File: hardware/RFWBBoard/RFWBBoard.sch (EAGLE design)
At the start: 123 parts, among them IC1 24LC025ST, J1 CON-71742-3003-BOT, M1 MOUNT-HOLE3.3, M2 MOUNT-HOLE3.3, M3 MOUNT-HOLE3.3, M4 MOUNT-HOLE3.3, M5 FIDUCIAL1X2, M6 FIDUCIAL1X2, M7 FIDUCIAL1X2, M8 FIDUCIAL1X2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

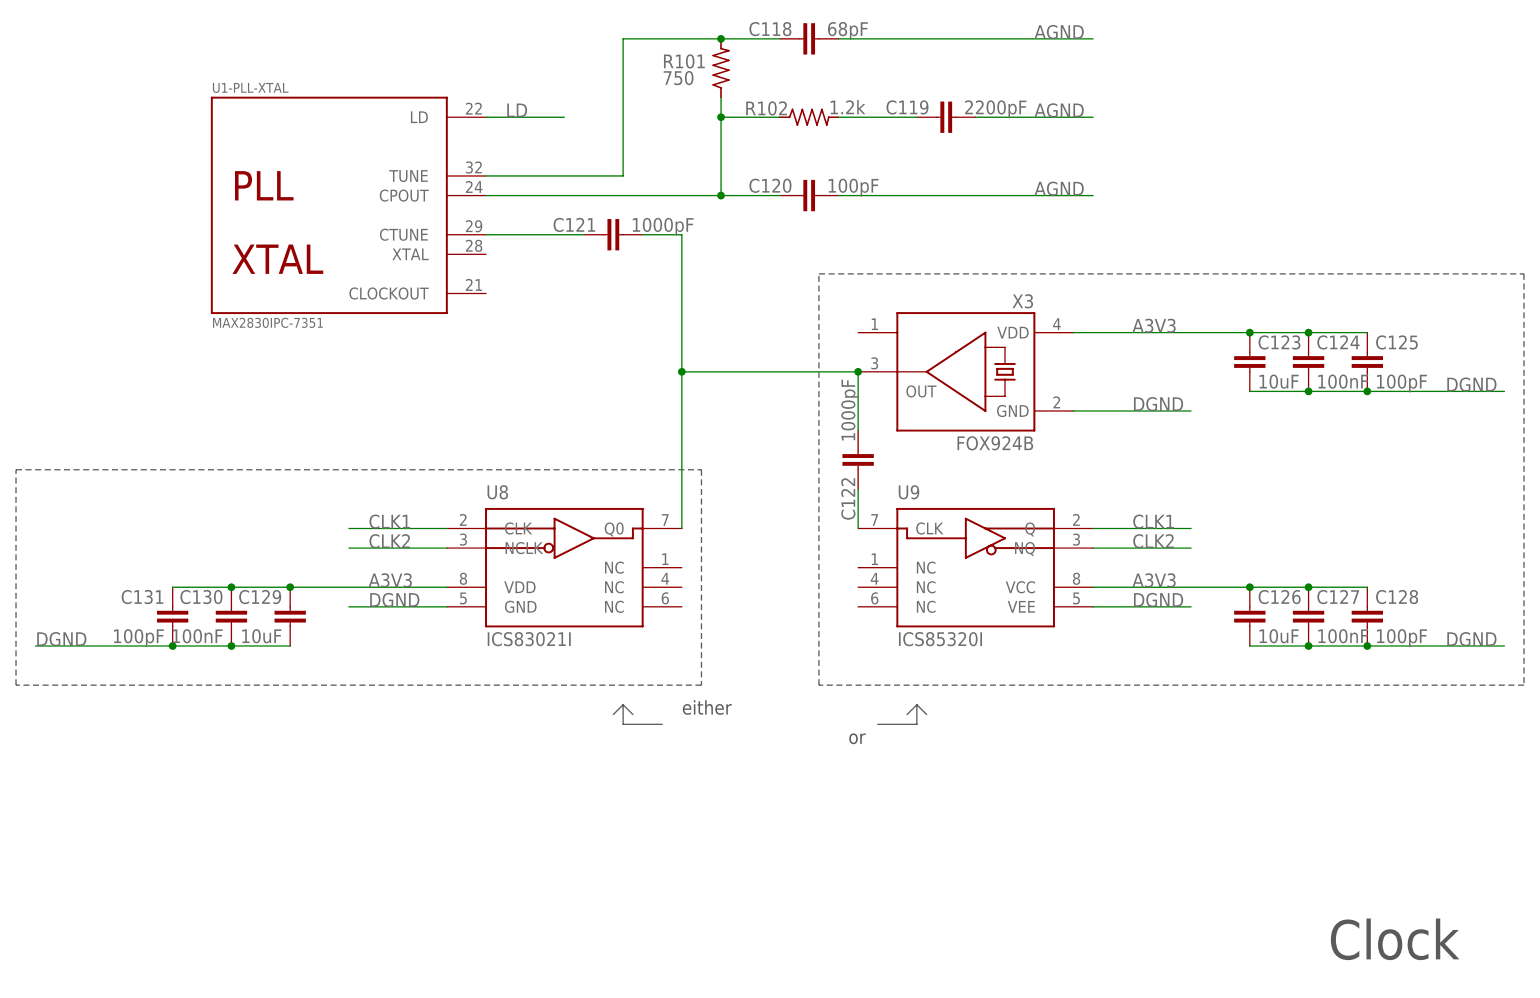
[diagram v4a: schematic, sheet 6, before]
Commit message: Errors corrected:
Radio Board

- External TCXO is connected to MAX2830 XTAL pin (28) instead of CTUNE pin (29)
- TCXO power supply digital, ground analog
- Mark for 1. pin for baluns not visible enough
- C105, C106 names covered by vias in documentation (PCB changed only)


Breakout Board

- 84 mezzanine connectors on top and bottom swapped


Power Board

- Silkscreen labels D1V5 and D3V3 are swapped
- VBUS measurement point not assembled
- SW2 name missing, needs caption (silk screen)
- Power input needs description (silk screen)
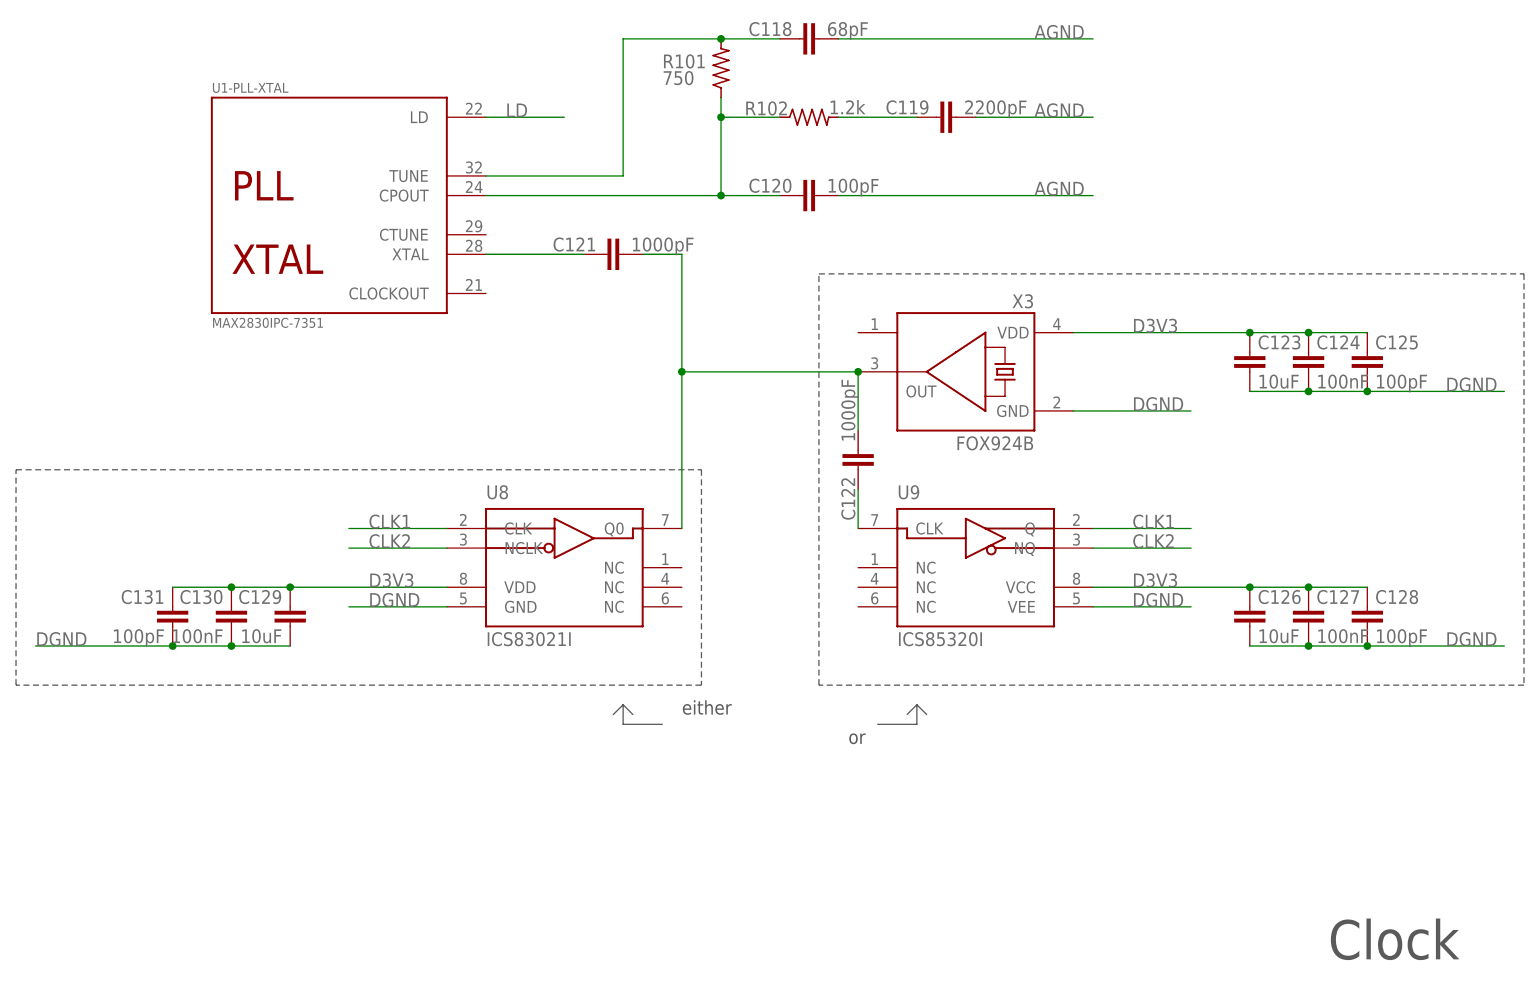
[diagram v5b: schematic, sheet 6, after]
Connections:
- net A3V3: no longer C123.1, C124.1, C125.1, C126.1, C127.1, C128.1, C129.1, C130.1, C131.1, U8.VDD, U9.VCC, X3.VCC
- net D3V3: now also C123.1, C124.1, C125.1, C126.1, C127.1, C128.1, C129.1, C130.1, C131.1, U8.VDD, U9.VCC, X3.VCC
- net N$6: now also U1-PLL-XTAL.XTAL; no longer U1-PLL-XTAL.CTUNE
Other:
- moved on the sheet: C121
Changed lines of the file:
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@@
 <attribute name="VALUE" x="130.81" y="129.921" size="1.778" layer="96"/>
 </instance>
-<instance part="C121" gate="G$1" x="101.6" y="114.3" smashed="yes" rot="R90">
-<attribute name="NAME" x="94.996" y="114.681" size="1.778" layer="95"/>
-<attribute name="VALUE" x="105.156" y="114.681" size="1.778" layer="96"/>
+<instance part="C121" gate="G$1" x="101.6" y="111.76" smashed="yes" rot="R90">
+<attribute name="NAME" x="94.996" y="112.141" size="1.778" layer="95"/>
+<attribute name="VALUE" x="105.156" y="112.141" size="1.778" layer="96"/>
 </instance>
 <instance part="X3" gate="G$1" x="149.86" y="96.52" rot="MR0"/>
@@
 </segment>
 </net>
-<net name="A3V3" class="0">
-<segment>
-<pinref part="X3" gate="G$1" pin="VCC"/>
-<wire x1="162.56" y1="101.6" x2="185.42" y2="101.6" width="0.1524" layer="91"/>
-<label x="170.18" y="101.6" size="1.778" layer="95"/>
-<pinref part="C125" gate="G$1" pin="1"/>
-<pinref part="C124" gate="G$1" pin="1"/>
-<wire x1="185.42" y1="101.6" x2="193.04" y2="101.6" width="0.1524" layer="91"/>
-<wire x1="193.04" y1="101.6" x2="200.66" y2="101.6" width="0.1524" layer="91"/>
-<junction x="193.04" y="101.6"/>
-<pinref part="C123" gate="G$1" pin="1"/>
-<junction x="185.42" y="101.6"/>
-</segment>
-<segment>
-<pinref part="U9" gate="G$1" pin="VCC"/>
-<wire x1="165.1" y1="68.58" x2="185.42" y2="68.58" width="0.1524" layer="91"/>
-<label x="170.18" y="68.58" size="1.778" layer="95"/>
-<pinref part="C128" gate="G$1" pin="1"/>
-<pinref part="C127" gate="G$1" pin="1"/>
-<wire x1="185.42" y1="68.58" x2="193.04" y2="68.58" width="0.1524" layer="91"/>
-<wire x1="193.04" y1="68.58" x2="200.66" y2="68.58" width="0.1524" layer="91"/>
-<junction x="193.04" y="68.58"/>
-<pinref part="C126" gate="G$1" pin="1"/>
-<junction x="185.42" y="68.58"/>
-</segment>
-<segment>
-<pinref part="U8" gate="G$1" pin="VDD"/>
-<wire x1="60.96" y1="68.58" x2="81.28" y2="68.58" width="0.1524" layer="91"/>
-<label x="71.12" y="68.58" size="1.778" layer="95"/>
-<pinref part="C131" gate="G$1" pin="1"/>
-<pinref part="C130" gate="G$1" pin="1"/>
-<wire x1="60.96" y1="68.58" x2="53.34" y2="68.58" width="0.1524" layer="91"/>
-<wire x1="53.34" y1="68.58" x2="45.72" y2="68.58" width="0.1524" layer="91"/>
-<junction x="53.34" y="68.58"/>
-<pinref part="C129" gate="G$1" pin="1"/>
-<junction x="60.96" y="68.58"/>
-</segment>
-</net>
 <net name="N$5" class="0">
 <segment>
@@
 <net name="N$6" class="0">
 <segment>
-<pinref part="U1" gate="-PLL-XTAL" pin="CTUNE"/>
 <pinref part="C121" gate="G$1" pin="1"/>
-<wire x1="86.36" y1="114.3" x2="99.06" y2="114.3" width="0.1524" layer="91"/>
+<wire x1="86.36" y1="111.76" x2="99.06" y2="111.76" width="0.1524" layer="91"/>
+<pinref part="U1" gate="-PLL-XTAL" pin="XTAL"/>
 </segment>
 </net>
@@
 <pinref part="C121" gate="G$1" pin="2"/>
 <pinref part="C122" gate="G$1" pin="2"/>
-<wire x1="111.76" y1="114.3" x2="106.68" y2="114.3" width="0.1524" layer="91"/>
+<wire x1="111.76" y1="111.76" x2="106.68" y2="111.76" width="0.1524" layer="91"/>
 <wire x1="134.62" y1="96.52" x2="134.62" y2="88.9" width="0.1524" layer="91"/>
 <pinref part="U8" gate="G$1" pin="Q0"/>
 <wire x1="111.76" y1="76.2" x2="111.76" y2="96.52" width="0.1524" layer="91"/>
-<wire x1="111.76" y1="96.52" x2="111.76" y2="114.3" width="0.1524" layer="91"/>
+<wire x1="111.76" y1="96.52" x2="111.76" y2="111.76" width="0.1524" layer="91"/>
 <junction x="111.76" y="96.52"/>
 <junction x="134.62" y="96.52"/>
@@
 </segment>
 </net>
+<net name="D3V3" class="0">
+<segment>
+<pinref part="U8" gate="G$1" pin="VDD"/>
+<wire x1="60.96" y1="68.58" x2="81.28" y2="68.58" width="0.1524" layer="91"/>
+<label x="71.12" y="68.58" size="1.778" layer="95"/>
+<pinref part="C131" gate="G$1" pin="1"/>
+<pinref part="C130" gate="G$1" pin="1"/>
+<wire x1="60.96" y1="68.58" x2="53.34" y2="68.58" width="0.1524" layer="91"/>
+<wire x1="53.34" y1="68.58" x2="45.72" y2="68.58" width="0.1524" layer="91"/>
+<junction x="53.34" y="68.58"/>
+<pinref part="C129" gate="G$1" pin="1"/>
+<junction x="60.96" y="68.58"/>
+</segment>
+<segment>
+<pinref part="U9" gate="G$1" pin="VCC"/>
+<wire x1="165.1" y1="68.58" x2="185.42" y2="68.58" width="0.1524" layer="91"/>
+<label x="170.18" y="68.58" size="1.778" layer="95"/>
+<pinref part="C128" gate="G$1" pin="1"/>
+<pinref part="C127" gate="G$1" pin="1"/>
+<wire x1="185.42" y1="68.58" x2="193.04" y2="68.58" width="0.1524" layer="91"/>
+<wire x1="193.04" y1="68.58" x2="200.66" y2="68.58" width="0.1524" layer="91"/>
+<junction x="193.04" y="68.58"/>
+<pinref part="C126" gate="G$1" pin="1"/>
+<junction x="185.42" y="68.58"/>
+</segment>
+<segment>
+<pinref part="X3" gate="G$1" pin="VCC"/>
+<wire x1="162.56" y1="101.6" x2="185.42" y2="101.6" width="0.1524" layer="91"/>
+<label x="170.18" y="101.6" size="1.778" layer="95"/>
+<pinref part="C125" gate="G$1" pin="1"/>
+<pinref part="C124" gate="G$1" pin="1"/>
+<wire x1="185.42" y1="101.6" x2="193.04" y2="101.6" width="0.1524" layer="91"/>
+<wire x1="193.04" y1="101.6" x2="200.66" y2="101.6" width="0.1524" layer="91"/>
+<junction x="193.04" y="101.6"/>
+<pinref part="C123" gate="G$1" pin="1"/>
+<junction x="185.42" y="101.6"/>
+</segment>
+</net>
